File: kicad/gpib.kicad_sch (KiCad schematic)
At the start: 8 parts, among them J2 Conn_02x13_Odd_Even, U120 74LS244, U163 74LS00, U164 74LS02, U85 8291A, U86 8292, U87 8293, U88 8293

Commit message: update kicad project
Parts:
- removed U120: 74LS244, Package_DIP:DIP-20_W7.62mm_Socket, symbol 74xx:74LS244
- added R38, R39: ??Ω, seequa_footprints:R_Seequa_Resistor, symbol Device:R_Small
- added U170: PAL16R6, Package_DIP:DIP-20_W7.62mm_Socket, symbol seequa:PAL16R6
- J2: seq_coord (none) -> I33
- U163: seq_coord (none) -> H33; seq_silkscreen (none) -> LS00
- U164: seq_coord (none) -> G33; seq_silkscreen (none) -> LS02
- U85: seq_coord (none) -> G30; seq_silkscreen (none) -> 8291
- U86: seq_coord (none) -> G31; seq_silkscreen (none) -> 8292
- U87: seq_coord (none) -> I30; seq_silkscreen (none) -> 8293
- U88: seq_coord (none) -> I31; seq_silkscreen (none) -> 8293
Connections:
- net +5V: now also U163.14 (VCC), U164.14 (VCC), U86.26 (V_{CC}), U86.40 (V_{CC}), U86.5 (V_{CC}), R38.1, R39.1, U170.20 (V_{CC})
- net at U163.7 (GND): now also U164.7 (GND), U85.20 (GND), U86.20 (V_{SS}), U86.7 (V_{SS}), U87.14 (GND), U87.20 (GND), U88.14 (GND), U88.20 (GND), U170.10 (GND)
- net ~{XIOW}: now reaches U86.10 (~{WR})
- net PD0: now reaches U86.12 (D0)
- net PD1: now reaches U86.13 (D1)
- net PD2: now reaches U86.14 (D2)
- net PD3: now reaches U86.15 (D3)
- net PD4: now reaches U86.16 (D4)
- net PD5: now reaches U86.17 (D5)
- net PD6: now reaches U86.18 (D6)
- net PD7: now reaches U86.19 (D7)
- net ~{8292_{RESET}}: now reaches U86.4 (~{RESET})
- net ~{XIOR}: now reaches U86.8 (~{RD})
- net XAT0: now reaches U86.9 (A0)
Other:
- moved on the sheet: J2, U163A, U163B, U163C, U163D, U163E, U164A, U164B, U164C, U164D, U164E, U85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

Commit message: More updates
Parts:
- removed unit 1 of U163
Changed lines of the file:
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@@
-	(symbol
-		(lib_id "74xx:74LS00")
-		(at 307.34 156.21 0)
-		(unit 1)
-		(exclude_from_sim no)
-		(in_bom yes)
-		(on_board yes)
-		(dnp no)
-		(fields_autoplaced yes)
-		(property "Reference" "U163"
-			(at 307.3317 147.32 0)
-			(effects
-				(font
-					(size 1.27 1.27)
-				)
-			)
-		)
-		(property "Value" "74LS00"
-			(at 307.3317 149.86 0)
-			(effects
-				(font
-					(size 1.27 1.27)
-				)
-			)
-		)
-		(property "Footprint" "Package_DIP:DIP-14_W7.62mm_Socket"
-			(at 307.34 156.21 0)
-			(effects
-				(font
-					(size 1.27 1.27)
-				)
-				(hide yes)
-			)
-		)
-		(property "Datasheet" "http://www.ti.com/lit/gpn/sn74ls00"
-			(at 307.34 156.21 0)
-			(effects
-				(font
-					(size 1.27 1.27)
-				)
-				(hide yes)
-			)
-		)
-		(property "Description" "quad 2-input NAND gate"
-			(at 307.34 156.21 0)
-			(effects
-				(font
-					(size 1.27 1.27)
-				)
-				(hide yes)
-			)
-		)
-		(property "seq_partno" ""
-			(at 307.34 156.21 0)
-			(effects
-				(font
-					(size 1.27 1.27)
-				)
-				(hide yes)
-			)
-		)
-		(property "seq_coord" "H33"
-			(at 307.34 156.21 0)
-			(effects
-				(font
-					(size 1.27 1.27)
-				)
-				(hide yes)
-			)
-		)
-		(property "seq_silkscreen" "LS00"
-			(at 307.34 156.21 0)
-			(effects
-				(font
-					(size 1.27 1.27)
-				)
-				(hide yes)
-			)
-		)
-		(property "seq_sharpie" ""
-			(at 307.34 156.21 0)
-			(effects
-				(font
-					(size 1.27 1.27)
-				)
-				(hide yes)
-			)
-		)
-		(property "seq_notes" ""
-			(at 307.34 156.21 0)
-			(effects
-				(font
-					(size 1.27 1.27)
-				)
-				(hide yes)
-			)
-		)
-		(property "seq_port" ""
-			(at 307.34 156.21 0)
-			(effects
-				(font
-					(size 1.27 1.27)
-				)
-				(hide yes)
-			)
-		)
-		(pin "1"
-		)
-		(pin "3"
-		)
-		(pin "6"
-		)
-		(pin "10"
-		)
-		(pin "4"
-		)
-		(pin "5"
-		)
-		(pin "2"
-		)
-		(pin "9"
-		)
-		(pin "8"
-		)
-		(pin "12"
-		)
-		(pin "13"
-		)
-		(pin "11"
-		)
-		(pin "14"
-		)
-		(pin "7"
-		)
-		(instances
-			(project ""
-				(path "/ae890d4c-6a02-4621-80ce-7ef4317218ea/cba7d65e-8a99-424a-8a83-a73d22837a36"
-					(reference "U163")
-					(unit 1)
-				)
-			)
-		)
-	)
 	(symbol
 		(lib_id "74xx:74LS00")

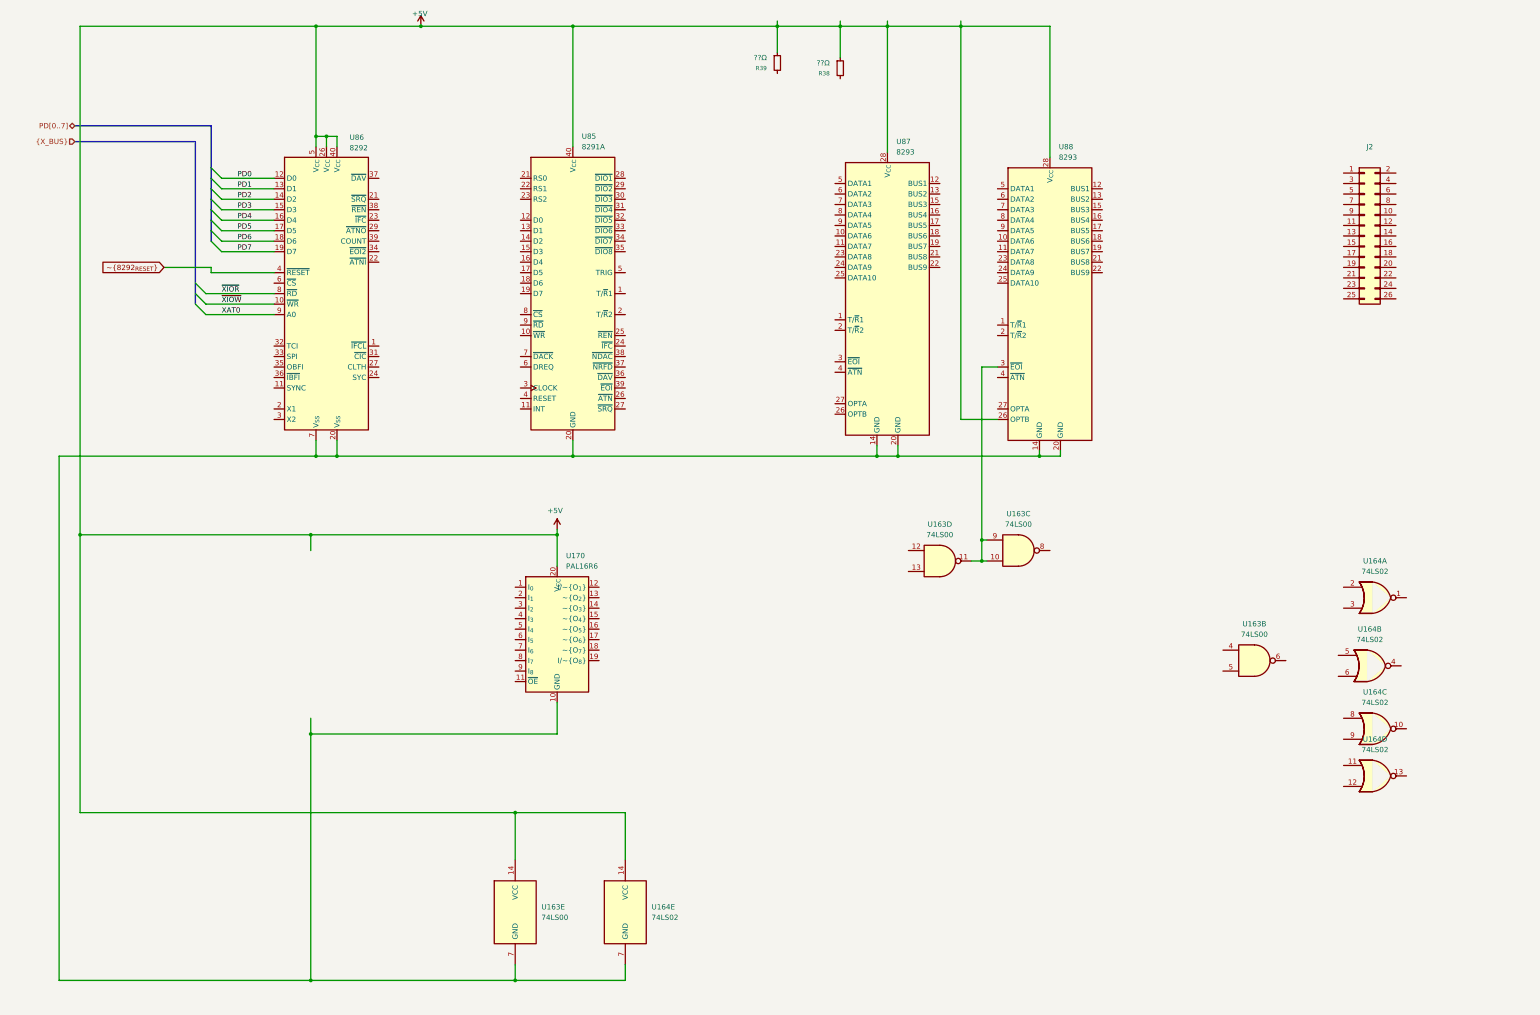
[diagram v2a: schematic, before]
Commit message: Add parallel port, game port
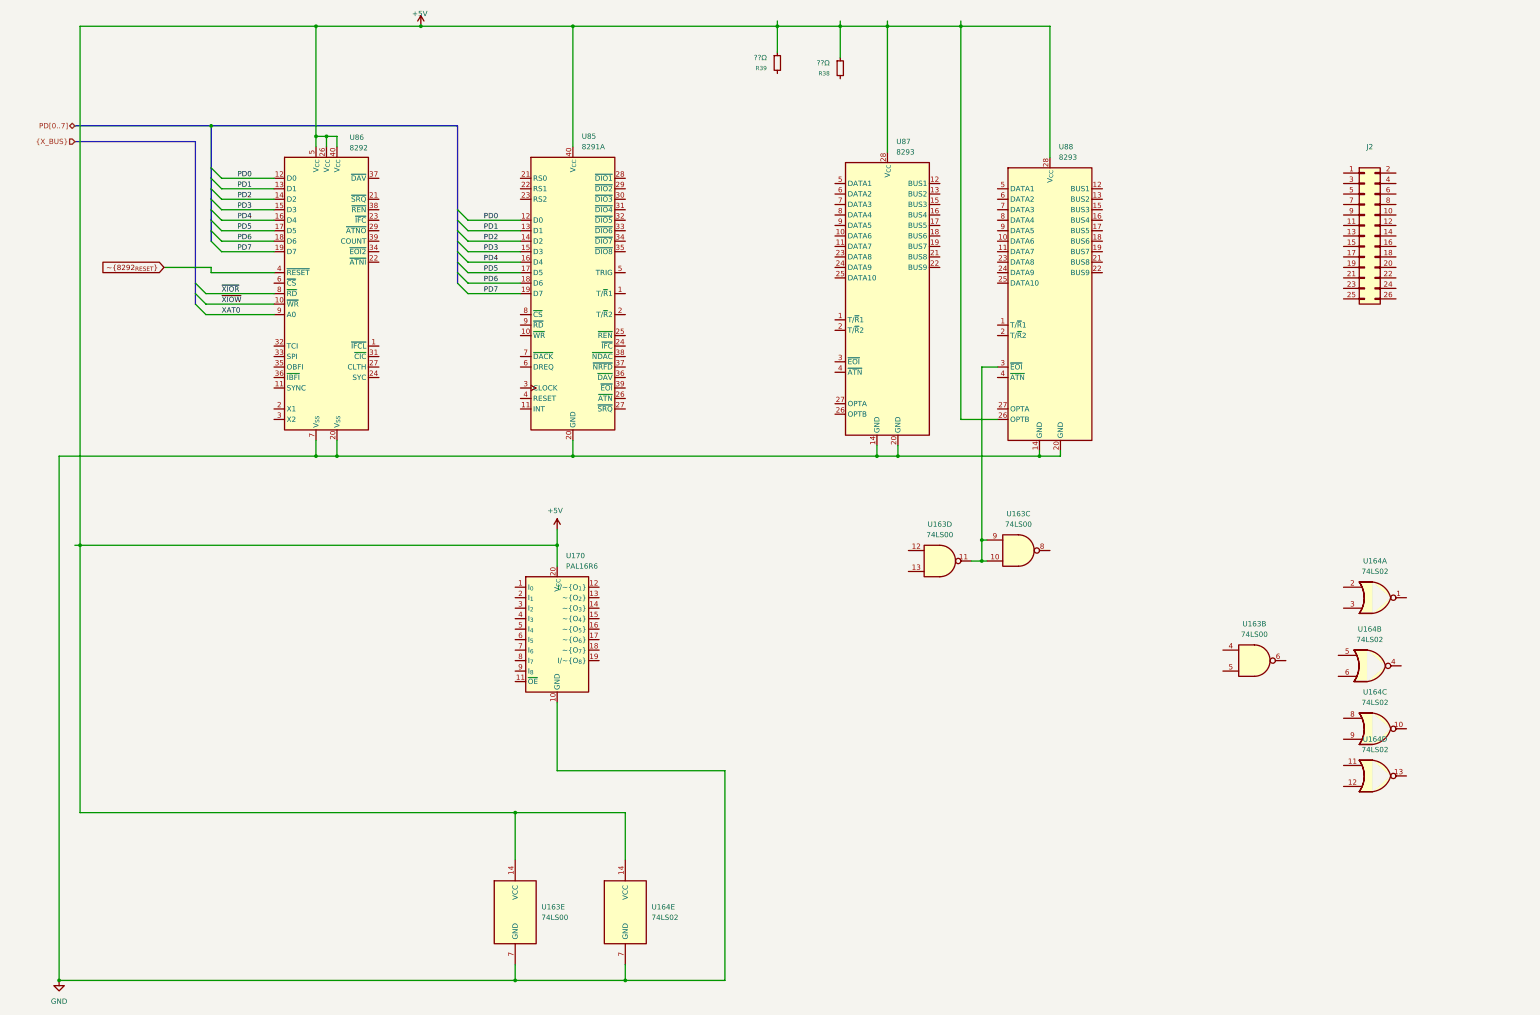
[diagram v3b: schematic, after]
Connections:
- net PD0: now also U85.12 (D0)
- net PD1: now also U85.13 (D1)
- net PD2: now also U85.14 (D2)
- net PD3: now also U85.15 (D3)
- net PD4: now also U85.16 (D4)
- net PD5: now also U85.17 (D5)
- net PD6: now also U85.18 (D6)
- net PD7: now also U85.19 (D7)
- net GND: now reaches U163.7 (GND), U164.7 (GND), U170.10 (GND), U85.20 (GND), U86.20 (V_{SS}), U86.7 (V_{SS}), U87.14 (GND), U87.20 (GND), U88.14 (GND), U88.20 (GND)

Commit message: A little work on composite output and GPIB
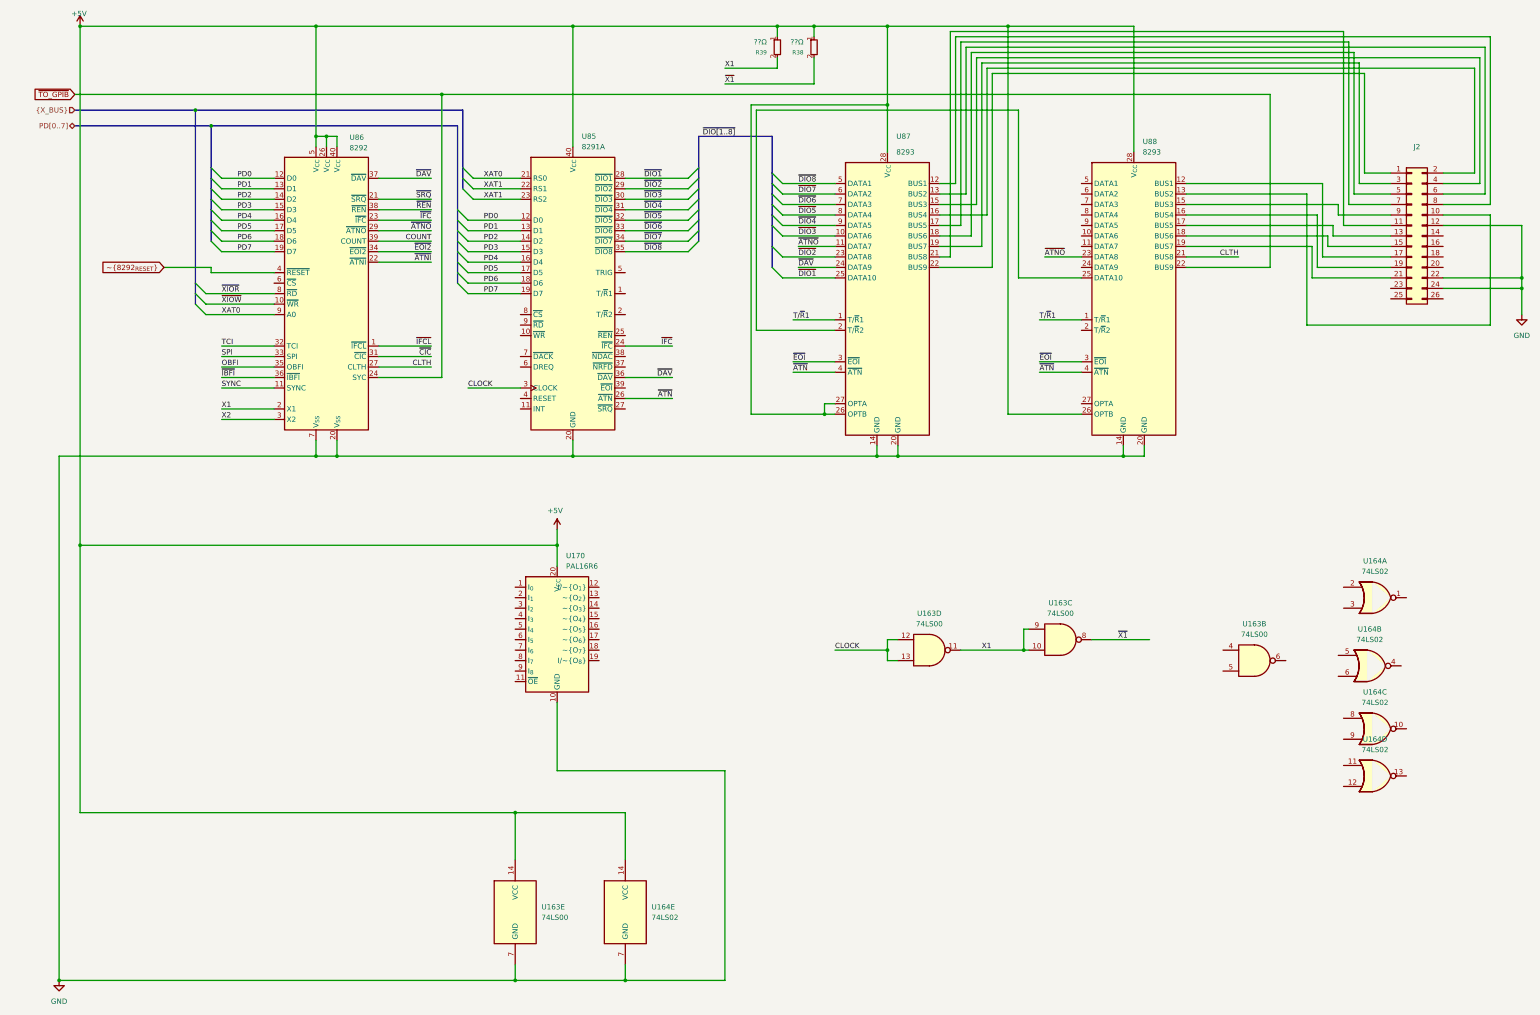
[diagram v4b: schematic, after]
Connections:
- net +5V: now also U87.26 (OPTB), U87.27 (OPTA)
- net GND: now also J2.12 (Pin_12), J2.22 (Pin_22), J2.24 (Pin_24)
- net XAT0: now also U85.21 (RS0)
- net X1: now reaches U163.10, U163.11, U163.9
- net X1: now also R39.2, U86.2 (X1); no longer U88.3 (~{EOI})
- net CLOCK: now reaches U163.12
- net CLOCK: now also U163.13, U85.3 (CLOCK)
- net XAT1: now reaches U85.22 (RS1)
- net XAT1: now also U85.23 (RS2)
- net ~{IFC}: now reaches U85.24 (~{IFC})
- net ~{IFC}: now also U86.23 (~{IFC})
- net ~{ATN}: now reaches U85.26 (~{ATN})
- net ~{ATN}: now also U87.4 (~{ATN}), U88.4 (~{ATN})
- net ~{DIO1}: now reaches U85.28 (~{DIO1})
- net ~{DIO1}: now also U87.25 (DATA10)
- net ~{DIO2}: now reaches U85.29 (~{DIO2})
- net ~{DIO2}: now also U87.23 (DATA8)
- net ~{DIO3}: now reaches U85.30 (~{DIO3})
- net ~{DIO3}: now also U87.10 (DATA6)
- net ~{DIO4}: now reaches U85.31 (~{DIO4})
- net ~{DIO4}: now also U87.9 (DATA5)
- net ~{DIO5}: now reaches U85.32 (~{DIO5})
- net ~{DIO5}: now also U87.8 (DATA4)
- net ~{DIO6}: now reaches U85.33 (~{DIO6})
- net ~{DIO6}: now also U87.7 (DATA3)
- net ~{DIO7}: now reaches U85.34 (~{DIO7})
- net ~{DIO7}: now also U87.6 (DATA2)
- net ~{DIO8}: now reaches U85.35 (~{DIO8})
- net ~{DIO8}: now also U87.5 (DATA1)
- net ~{DAV}: now reaches U85.36 (~{DAV})
- net ~{DAV}: now also U86.37 (~{DAV}), U87.24 (DATA9)
- net ~{X1}: now reaches R38.2
- net ~{X1}: now also U163.8
- net ~{IFCL}: now reaches U86.1 (~{IFCL})
- net SYNC: now reaches U86.11 (SYNC)
- net ~{SRQ}: now reaches U86.21 (~{SRQ})
- net ~{ATNI}: now reaches U86.22 (~{ATNI})
- net ~{TO_GPIB}: now reaches U86.24 (SYC)
- net ~{TO_GPIB}: now also U88.22 (BUS9)
- net CLTH: now reaches U86.27 (CLTH)
- net CLTH: now also U88.21 (BUS8)
- net ~{ATNO}: now reaches U86.29 (~{ATNO})
- net ~{ATNO}: now also U87.11 (DATA7), U88.23 (DATA8)
- net X2: now reaches U86.3 (X2)
- net ~{CIC}: now reaches U86.31 (~{CIC})
- net TCI: now reaches U86.32 (TCI)
- net SPI: now reaches U86.33 (SPI)
- net ~{EOI2}: now reaches U86.34 (~{EOI2})
- net OBFI: now reaches U86.35 (OBFI)
- net ~{IBFI}: now reaches U86.36 (~{IBFI})
- net ~{REN}: now reaches U86.38 (~{REN})
- net COUNT: now reaches U86.39 (COUNT)
- net T/~{R}1: now reaches U87.1 (T/~{R}1)
- net T/~{R}1: now also U88.1 (T/~{R}1)
- net at U87.12 (BUS1): now also J2.8 (Pin_8)
- net at U87.13 (BUS2): now also J2.6 (Pin_6)
- net at U87.15 (BUS3): now also J2.4 (Pin_4)
- net at U87.16 (BUS4): now also J2.2 (Pin_2)
- net at U87.17 (BUS5): now also J2.7 (Pin_7)
- net at U87.18 (BUS6): now also J2.5 (Pin_5)
- net at U87.19 (BUS7): now also J2.3 (Pin_3)
- net at U87.2 (T/~{R}2): now also U88.25 (DATA10)
- net at U87.21 (BUS8): now also J2.11 (Pin_11)
- net at U87.22 (BUS9): now also J2.1 (Pin_1)
- net ~{EOI}: now reaches U87.3 (~{EOI})
- net ~{EOI}: now also U88.3 (~{EOI})
- net at J2.10 (Pin_10): now also U88.13 (BUS2)
- net at J2.13 (Pin_13): now also U88.17 (BUS5)
- net at J2.15 (Pin_15): now also U88.18 (BUS6)
- net at J2.17 (Pin_17): now also U88.12 (BUS1)
- net at J2.19 (Pin_19): now also U88.16 (BUS4)
- net at J2.21 (Pin_21): now also U88.19 (BUS7)
- net at J2.9 (Pin_9): now also U88.15 (BUS3)
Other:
- moved on the sheet: J2, U163C, U163D, U88
